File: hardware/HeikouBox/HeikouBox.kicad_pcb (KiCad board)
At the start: 2 copper layers, 100 x 100 mm, 192 parts, among them J101 5V, J201 Conn_02x05_Odd_Even, J202 Conn_02x08_Odd_Even, J301 DB15_Female_HighDensity_Mount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, J302 AudioJack3_SwitchTR, J501 Micro_SD_Card_TFP09-2-12B, J502 RGB, J503 PS/2, Q301 MMBT3904, Q302 MMBT3904, Q303 MMBT3904, Q304 MMBT3904, Q305 MMBT3904, Q306 MMBT3904, Q307 MMBT3904, Q501 BSS138, Q502 BSS138, Q503 BSS138, SW501 Left, SW502 Up, SW503 Down, SW504 Right, U101 LD1117S33TR, U102 LD1117S25TR, U103 LD1117S12TR, U201 HeikouBox-Core, U202 74HCU04, U401 K4S281632-UC60, U501 STM32-BluePill-Socket, Y201 14.31818MHz, Y202 28.37516MHz

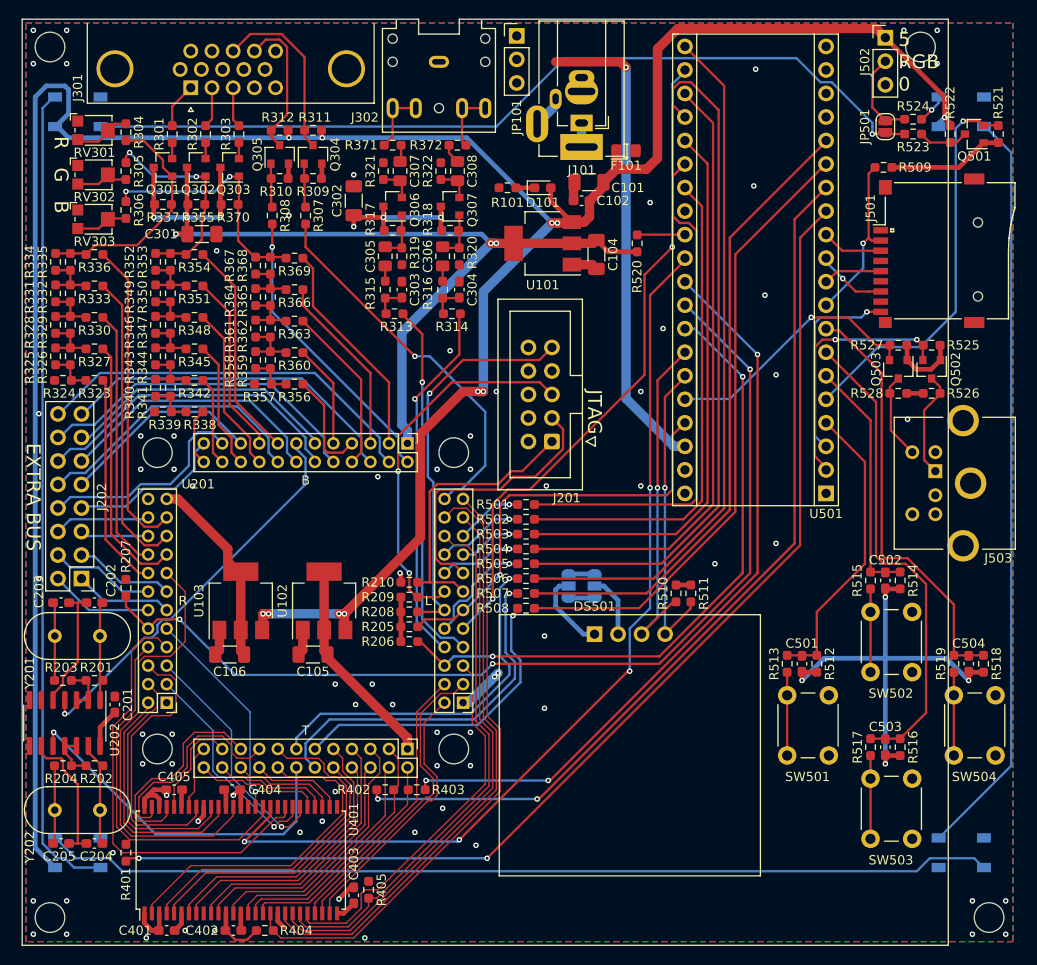
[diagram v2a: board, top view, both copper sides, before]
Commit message: Rerouted some logic
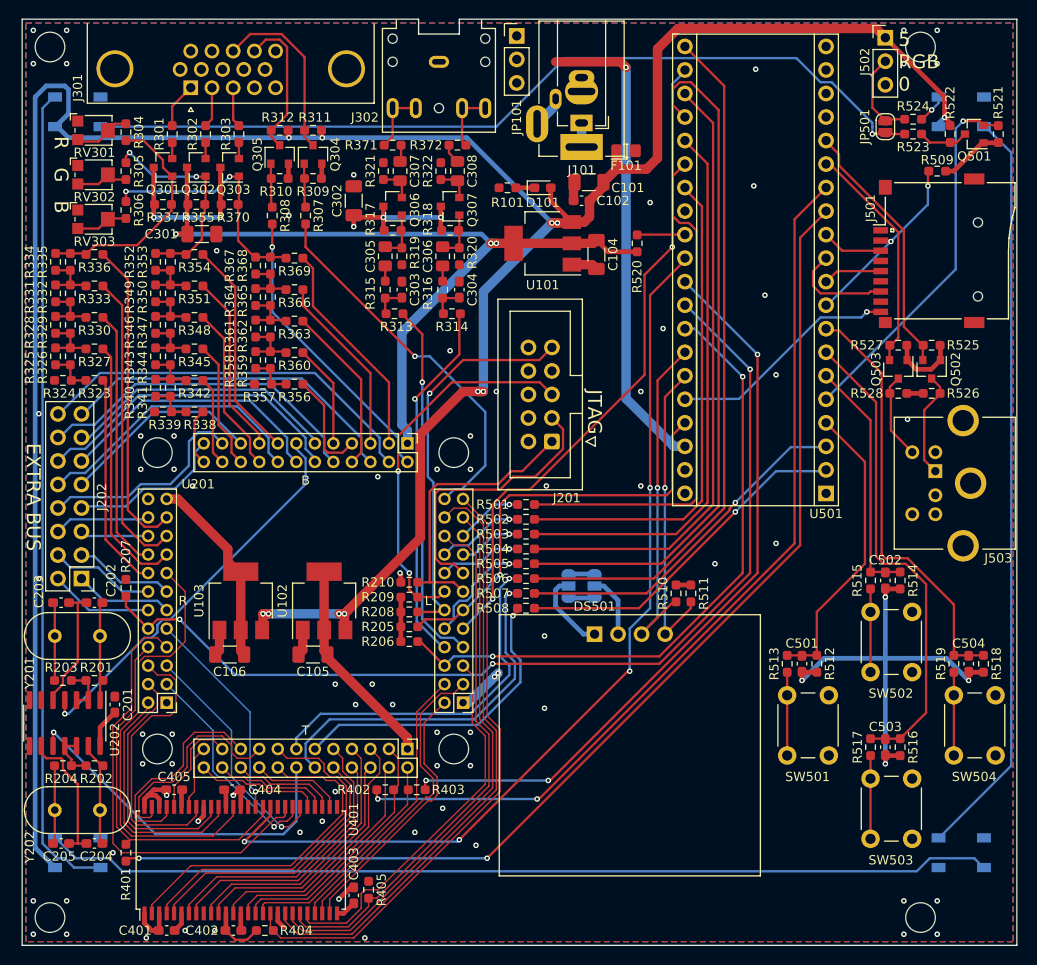
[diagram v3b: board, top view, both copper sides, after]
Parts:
- moved MH4 7.40 mm to (185.8, 153.8)
- moved R509 5.81 mm to (187.6, 73.2)
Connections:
- U501 pad 15: Net-(R508-Pad1) -> Net-(Q503-Pad2)
- U501 pad 16: Net-(R507-Pad1) -> Net-(Q502-Pad2)
- U501 pad 2: Net-(Q502-Pad2) -> Net-(R508-Pad1)
- U501 pad 3: Net-(J501-Pad9) -> Net-(R507-Pad1)
- U501 pad 36: Net-(Q503-Pad2) -> Net-(J501-Pad9)
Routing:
- net Net-(R507-Pad1): track 69.0 -> 38.3 mm, vias 0 -> 1
- net Net-(R508-Pad1): track 67.6 -> 37.7 mm, vias 0 -> 1
- net /part1-power/3V3: track 214.7 -> 209.0 mm
- net Net-(J501-Pad7): track 7.63 -> 11.3 mm, vias 1 -> 0
- net Net-(J501-Pad9): track 21.5 -> 25.1 mm
- net Net-(Q503-Pad2): track 28.6 -> 25.1 mm, vias 1 -> 0
- net Net-(Q501-Pad2): track 42.9 -> 40.2 mm
- net Net-(J501-Pad2): track 18.5 -> 20.3 mm, vias 1 -> 2
- net Net-(Q502-Pad2): track 27.6 -> 28.2 mm, vias 2 -> 0
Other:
- board size 100 x 100 mm -> 107.4 x 100 mm

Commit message: Mainboard v0.1 PCB ready for export
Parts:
- removed the C502 at (182.0, 117.4)
- removed J502: RGB, Connector_PinHeader_2.54mm:PinHeader_1x03_P2.54mm_Vertical
- removed JP101: Power, Connector_PinHeader_2.54mm:PinHeader_1x03_P2.54mm_Vertical
- removed JP501: RGB Bypass, Jumper:SolderJumper-2_P1.3mm_Open_RoundedPad1.0x1.5mm
- removed Q501: BSS138, Package_TO_SOT_SMD:SOT-23
- removed R401, R402, R403, R404, R405: 1K, Resistor_SMD:R_0603_1608Metric_Pad0.98x0.95mm_HandSolder
- removed the R516 at (183.6, 135.4)
- removed the R517 at (180.4, 135.4)
- added C504: 100n, Capacitor_SMD:C_0603_1608Metric_Pad1.08x0.95mm_HandSolder, F.Cu at (174.2, 146.6)
- added D102: D, Diode_SMD:D_SOD-123, F.Cu at (141.6, 63.8)
- added D103: 5.6V, Diode_SMD:D_SOD-123, F.Cu at (169.6, 80.4)
- added F102: Poly 200mA, Fuse:Fuse_0805_2012Metric_Pad1.15x1.40mm_HandSolder, F.Cu at (141.6, 59.4)
- added R518: 10K, Resistor_SMD:R_0603_1608Metric_Pad0.98x0.95mm_HandSolder, F.Cu at (172.4, 148.2)
- added R519: 1K, Resistor_SMD:R_0603_1608Metric_Pad0.98x0.95mm_HandSolder, F.Cu at (170.8, 146.6)
- added R529: 100R, Resistor_SMD:R_0603_1608Metric_Pad0.98x0.95mm_HandSolder, F.Cu at (185.8, 130.8)
- added R530: 1K, Resistor_SMD:R_0603_1608Metric_Pad0.98x0.95mm_HandSolder, F.Cu at (161.2, 118.2)
- added R531: 1K, Resistor_SMD:R_0603_1608Metric_Pad0.98x0.95mm_HandSolder, F.Cu at (159.6, 118.2)
- F101: value Poly 1A -> Poly 2A; footprint Fuse:Fuse_0805_2012Metric_Pad1.15x1.40mm_HandSolder -> Fuse:Fuse_1206_3216Metric_Pad1.42x1.75mm_HandSolder
- R101: value 1K -> 330R
- R520: value RUSB -> 1K5
- R522: value 1K -> 10K
- R524: value 1K -> 100R
- moved R524 59.6 mm to (185.8, 127.2), turned to 270 degrees
- moved R521 55.6 mm to (138.8, 73.6)
- moved R522 50.8 mm to (138.8, 77.0), turned to 270 degrees
- moved R512 45.2 mm to (137.8, 152.6)
- moved R514 45.2 mm to (155.8, 152.6)
- moved R513 42.5 mm to (139.4, 154.4)
- moved R515 42.5 mm to (157.4, 154.4)
- moved C501 41.6 mm to (139.4, 151.0), turned to 270 degrees
- moved C502 41.6 mm to (157.4, 151.0), turned to 270 degrees
- moved R101 39.4 mm to (180.6, 76.2), turned to 90 degrees
- moved R527 39.0 mm to (179.0, 130.8), turned to 90 degrees
- moved Q503 36.2 mm to (181.6, 130.8), turned to 0 degrees
- moved R525 36.1 mm to (179.0, 127.2), turned to 90 degrees
- moved D101 35.9 mm to (180.6, 79.8), turned to 270 degrees
- moved R523 34.2 mm to (167.8, 98.8), turned to 270 degrees
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- renumbered C504 to C502, R518 to R514, R519 to R515, R514 to R516, R515 to R517, SW504 to SW502, SW502 to SW503, SW503 to SW504
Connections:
- net Net-(J501-Pad3) renamed /part5-hub/SD_MOSI
- net Net-(J501-Pad5) renamed /part5-hub/SD_SCK
- net Net-(J501-Pad7) renamed /part5-hub/SD_MISO
- net Net-(R505-Pad1) renamed /part5-hub/MDB4_CD_R
- net Net-(R520-Pad1) renamed /part5-hub/USB_DP
- C501 pad 1: /part1-power/3V3 -> /part5-hub/3V3_HUB
- C501 pad 2: Net-(C501-Pad2) -> /part5-hub/BUTTON_L
- C502 pad 1: /part1-power/3V3 -> /part5-hub/3V3_HUB
- C502 pad 2: Net-(C504-Pad2) -> /part5-hub/BUTTON_R
- C503 pad 1: /part1-power/3V3 -> /part5-hub/3V3_HUB
- C503 pad 2: Net-(C503-Pad2) -> /part5-hub/BUTTON_U
- D101 pad 2: /part1-power/5V -> /part1-power/3V3
- D501 pad 1: /part1-power/5V -> /part1-power/3V3
- D502 pad 1: /part1-power/5V -> /part1-power/3V3
- D503 pad 1: /part1-power/5V -> /part1-power/3V3
- D504 pad 1: /part1-power/5V -> /part1-power/3V3
- DS501 pad 3: Net-(DS501-Pad3) -> /part5-hub/OLED_SCL
- DS501 pad 4: Net-(DS501-Pad4) -> /part5-hub/OLED_SDA
- F101 pad 1: /part1-power/5V -> Net-(F101-Pad1)
- F101 pad 2: Net-(F101-Pad2) -> /part1-power/5V
- J101 pad 1: Net-(J101-Pad1) -> Net-(F101-Pad1)
- J501 pad 2: Net-(J501-Pad2) -> /part5-hub/SD_SS
- J501 pad 4: /part1-power/3V3 -> /part5-hub/3V3_HUB
- J501 pad 9: Net-(J501-Pad9) -> /part5-hub/SD_DET
- JP502 pad 1: /part1-power/3V3 -> /part5-hub/3V3_HUB
- JP502 pad 2: Net-(DS501-Pad2) -> Net-(DS501-Pad1)
- JP503 pad 2: Net-(DS501-Pad1) -> Net-(DS501-Pad2)
- JP503 pad 3: /part1-power/3V3 -> /part5-hub/3V3_HUB
- Q306 pad 1: Net-(C305-Pad1) -> Net-(C305-Pad2)
- Q306 pad 2: Net-(C307-Pad2) -> Net-(C307-Pad1)
- Q307 pad 1: Net-(C306-Pad1) -> Net-(C306-Pad2)
- Q307 pad 2: Net-(C308-Pad2) -> Net-(C308-Pad1)
- Q502 pad 2: Net-(Q502-Pad2) -> /part5-hub/KEYBOARD_DAT
- Q502 pad 3: Net-(J503-Pad1) -> Net-(Q502-Pad3)
- Q503 pad 2: Net-(Q503-Pad2) -> /part5-hub/KEYBOARD_CLK
- Q503 pad 3: Net-(J503-Pad5) -> Net-(Q503-Pad3)
- R301 pad 1: Net-(J301-Pad1) -> Net-(Q301-Pad2)
- R301 pad 2: Net-(Q301-Pad2) -> Net-(J301-Pad1)
- R302 pad 1: Net-(J301-Pad2) -> Net-(Q302-Pad2)
- R302 pad 2: Net-(Q302-Pad2) -> Net-(J301-Pad2)
- R303 pad 1: Net-(J301-Pad3) -> Net-(Q303-Pad2)
- R303 pad 2: Net-(Q303-Pad2) -> Net-(J301-Pad3)
- R307 pad 1: Net-(Q304-Pad1) -> /part3-av/NHSYNC
- R307 pad 2: /part3-av/NHSYNC -> Net-(Q304-Pad1)
- R308 pad 1: Net-(Q305-Pad1) -> /part3-av/NVSYNC
- R308 pad 2: /part3-av/NVSYNC -> Net-(Q305-Pad1)
- R309 pad 1: /part1-power/GND -> Net-(Q304-Pad1)
- R309 pad 2: Net-(Q304-Pad1) -> /part1-power/GND
- R310 pad 1: /part1-power/GND -> Net-(Q305-Pad1)
- R310 pad 2: Net-(Q305-Pad1) -> /part1-power/GND
- R311 pad 1: Net-(J301-Pad13) -> /part1-power/3V3
- R311 pad 2: /part1-power/5V -> Net-(J301-Pad13)
- R312 pad 1: Net-(J301-Pad14) -> /part1-power/3V3
- R312 pad 2: /part1-power/5V -> Net-(J301-Pad14)
- R313 pad 1: Net-(C303-Pad1) -> /part3-av/LSIGMA
- R313 pad 2: /part3-av/LSIGMA -> Net-(C303-Pad1)
- R314 pad 1: Net-(C304-Pad1) -> /part3-av/RSIGMA
- R314 pad 2: /part3-av/RSIGMA -> Net-(C304-Pad1)
- R315 pad 1: Net-(C305-Pad2) -> Net-(C303-Pad1)
- R315 pad 2: Net-(C303-Pad1) -> Net-(C305-Pad1)
- R316 pad 1: Net-(C306-Pad2) -> Net-(C304-Pad1)
- R316 pad 2: Net-(C304-Pad1) -> Net-(C306-Pad1)
- R317 pad 2: Net-(C305-Pad1) -> Net-(C305-Pad2)
- R318 pad 2: Net-(C306-Pad1) -> Net-(C306-Pad2)
- R319 pad 1: Net-(C305-Pad1) -> Net-(C305-Pad2)
- R320 pad 1: Net-(C306-Pad1) -> Net-(C306-Pad2)
- R321 pad 1: Net-(C307-Pad2) -> Net-(C307-Pad1)
- R322 pad 1: Net-(C308-Pad2) -> Net-(C308-Pad1)
- R371 pad 1: Net-(J302-PadT) -> Net-(C307-Pad2)
- R371 pad 2: Net-(C307-Pad1) -> Net-(J302-PadT)
- R372 pad 1: Net-(J302-PadR) -> Net-(C308-Pad2)
- R372 pad 2: Net-(C308-Pad1) -> Net-(J302-PadR)
- R501 pad 1: Net-(R501-Pad1) -> /part5-hub/MDB0_RX_R
- R502 pad 1: Net-(R502-Pad1) -> /part5-hub/MDB1_TX_R
- R503 pad 1: Net-(R503-Pad1) -> /part5-hub/MDB2_R
- R504 pad 1: Net-(R504-Pad1) -> /part5-hub/MDB3_R
- R506 pad 1: Net-(R506-Pad1) -> /part5-hub/MDB5_R
- R507 pad 1: Net-(R507-Pad1) -> /part5-hub/MDB6_R
- R508 pad 1: Net-(R508-Pad1) -> /part5-hub/MDB7_R
- R509 pad 1: Net-(J501-Pad2) -> /part5-hub/3V3_HUB
- R509 pad 2: /part1-power/3V3 -> /part5-hub/SD_SS
- R510 pad 1: Net-(DS501-Pad3) -> /part5-hub/OLED_SCL
- R510 pad 2: /part1-power/3V3 -> /part5-hub/3V3_HUB
- R511 pad 1: Net-(DS501-Pad4) -> /part5-hub/OLED_SDA
- R511 pad 2: /part1-power/3V3 -> /part5-hub/3V3_HUB
- R512 pad 1: /part1-power/3V3 -> Net-(R512-Pad1)
- R512 pad 2: Net-(C501-Pad2) -> /part5-hub/3V3_HUB
- R513 pad 1: Net-(R513-Pad1) -> Net-(R512-Pad1)
- R513 pad 2: Net-(C501-Pad2) -> /part5-hub/BUTTON_L
- R514 pad 1: /part1-power/3V3 -> Net-(R514-Pad1)
- R514 pad 2: Net-(C504-Pad2) -> /part5-hub/3V3_HUB
- R515 pad 1: Net-(R519-Pad1) -> Net-(R514-Pad1)
- R515 pad 2: Net-(C504-Pad2) -> /part5-hub/BUTTON_R
- R516 pad 1: /part1-power/3V3 -> Net-(R516-Pad1)
- R516 pad 2: Net-(C502-Pad2) -> /part5-hub/3V3_HUB
- R517 pad 1: Net-(R515-Pad1) -> Net-(R516-Pad1)
- R517 pad 2: Net-(C502-Pad2) -> /part5-hub/BUTTON_U
- R520 pad 2: /part1-power/3V3 -> /part5-hub/3V3_HUB
- R521 pad 1: Net-(Q501-Pad2) -> /part1-power/3V3
- R521 pad 2: /part1-power/3V3 -> /part5-hub/PWR_DET
- R522 pad 1: Net-(Q501-Pad3) -> /part5-hub/PWR_DET
- R522 pad 2: /part1-power/5V -> /part1-power/GND
- R523 pad 1: Net-(Q501-Pad3) -> /part5-hub/NEOPIXEL
- R524 pad 1: Net-(D504-Pad2) -> Net-(Q502-Pad3)
- R524 pad 2: Net-(J502-Pad2) -> Net-(J503-Pad1)
- R525 pad 1: Net-(Q502-Pad2) -> /part5-hub/KEYBOARD_DAT
- R526 pad 1: Net-(J503-Pad1) -> Net-(Q502-Pad3)
- R527 pad 1: Net-(Q503-Pad2) -> /part5-hub/KEYBOARD_CLK
- R528 pad 1: Net-(J503-Pad5) -> Net-(Q503-Pad3)
- SW501 pad 1: Net-(R513-Pad1) -> Net-(R512-Pad1)
- SW502 pad 1: Net-(R519-Pad1) -> Net-(R514-Pad1)
- SW503 pad 1: Net-(R515-Pad1) -> Net-(R516-Pad1)
- U401 pad 37: /part4-memory/CKE -> /part1-power/3V3
- U501 pad 13: /part4-memory/XCLK -> /part5-hub/BUTTON_L
- U501 pad 14: /part4-memory/XWE -> /part5-hub/BUTTON_R
- U501 pad 15: Net-(Q503-Pad2) -> /part5-hub/BUTTON_U
- U501 pad 16: Net-(Q502-Pad2) -> /part5-hub/BUTTON_D
- U501 pad 2: Net-(R508-Pad1) -> Net-(U501-Pad2)
- U501 pad 21: Net-(R506-Pad1) -> /part2-core/cfg_NCFG
- U501 pad 23: Net-(R504-Pad1) -> /part5-hub/CFG_DONE_R
- U501 pad 25: Net-(R503-Pad1) -> /part5-hub/SD_DET
- U501 pad 26: Net-(R501-Pad1) -> /part5-hub/PWR_DET
- U501 pad 27: Net-(R502-Pad1) -> /part5-hub/MDB2_R
- U501 pad 3: Net-(R507-Pad1) -> Net-(U501-Pad3)
- U501 pad 30: /part4-memory/CKE -> /part5-hub/MDB3_R
- U501 pad 31: /part4-memory/XCAS -> /part5-hub/MDB5_R
- U501 pad 32: /part2-core/cfg_DONE -> /part5-hub/MDB6_R
- U501 pad 33: /part2-core/cfg_NSTAT -> /part5-hub/MDB7_R
- U501 pad 34: Net-(DS501-Pad3) -> /part5-hub/MDB0_RX_R
- U501 pad 35: Net-(DS501-Pad4) -> /part5-hub/MDB1_TX_R
- U501 pad 36: Net-(J501-Pad9) -> /part5-hub/OLED_SCL
- U501 pad 37: /part2-core/cfg_NCFG -> /part5-hub/OLED_SDA
- U501 pad 4: Net-(C501-Pad2) -> Net-(U501-Pad4)
- U501 pad 40: Net-(U501-Pad40) -> /part5-hub/3V3_HUB
- U501 pad 5: Net-(Q501-Pad2) -> /part5-hub/NEOPIXEL
- U501 pad 6: Net-(C502-Pad2) -> /part5-hub/KEYBOARD_DAT
- U501 pad 7: Net-(C503-Pad2) -> /part5-hub/KEYBOARD_CLK
- U501 pad 8: Net-(C504-Pad2) -> /part5-hub/CFG_NSTAT_R
- U501 pad 9: Net-(J501-Pad2) -> /part5-hub/SD_SS
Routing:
- net /part1-power/3V3: track 209.0 -> 533.3 mm, vias 13 -> 28
- net /part5-hub/3V3_HUB: track 0.00 -> 196.8 mm, vias 0 -> 10
- net /part4-memory/XCLK: track 124.2 -> 0.00 mm, vias 2 -> 0
- net /part4-memory/CKE: track 101.2 -> 0.00 mm, vias 4 -> 0
- net /part4-memory/XWE: track 97.3 -> 0.00 mm, vias 2 -> 0
- net /part5-hub/BUTTON_L: track 0.00 -> 92.1 mm, vias 0 -> 1
- net /part5-hub/BUTTON_R: track 0.00 -> 87.7 mm, vias 0 -> 1
- net /part5-hub/BUTTON_D: track 0.00 -> 82.7 mm, vias 0 -> 1
- net /part1-power/5V: track 295.6 -> 213.0 mm, vias 11 -> 7
- net /part4-memory/XCAS: track 80.8 -> 0.00 mm, vias 3 -> 0
- net Net-(R506-Pad1): track 75.2 -> 0.00 mm
- net Net-(R504-Pad1): track 66.9 -> 0.00 mm
- net /part5-hub/BUTTON_U: track 0.00 -> 63.6 mm, vias 0 -> 1
- net /part5-hub/SD_DET: track 0.00 -> 60.4 mm, vias 0 -> 1
- net Net-(R503-Pad1): track 60.2 -> 0.00 mm
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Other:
- board size 107.4 x 100 mm -> 100 x 100 mm
- board text added: "5V 2A"
- board text added: "GND VCC"
- board text added: "HeikouBox"
- board text added: "JLCJLCJLCJLC"
- board text added: "LINE AUD"
- board text added: "Mainboard v0.1 KasamiKona 2022"
- board text added: "SD CARD"
- board text added: "VGA VIDEO"
- board text removed: "5 RGB 0"
- board text removed: "5V 1A"
- board text removed: "LINE OUT"
- board text removed: "MICRO SD"
- board text removed: "VCC GND"
- board text removed: "VGA"

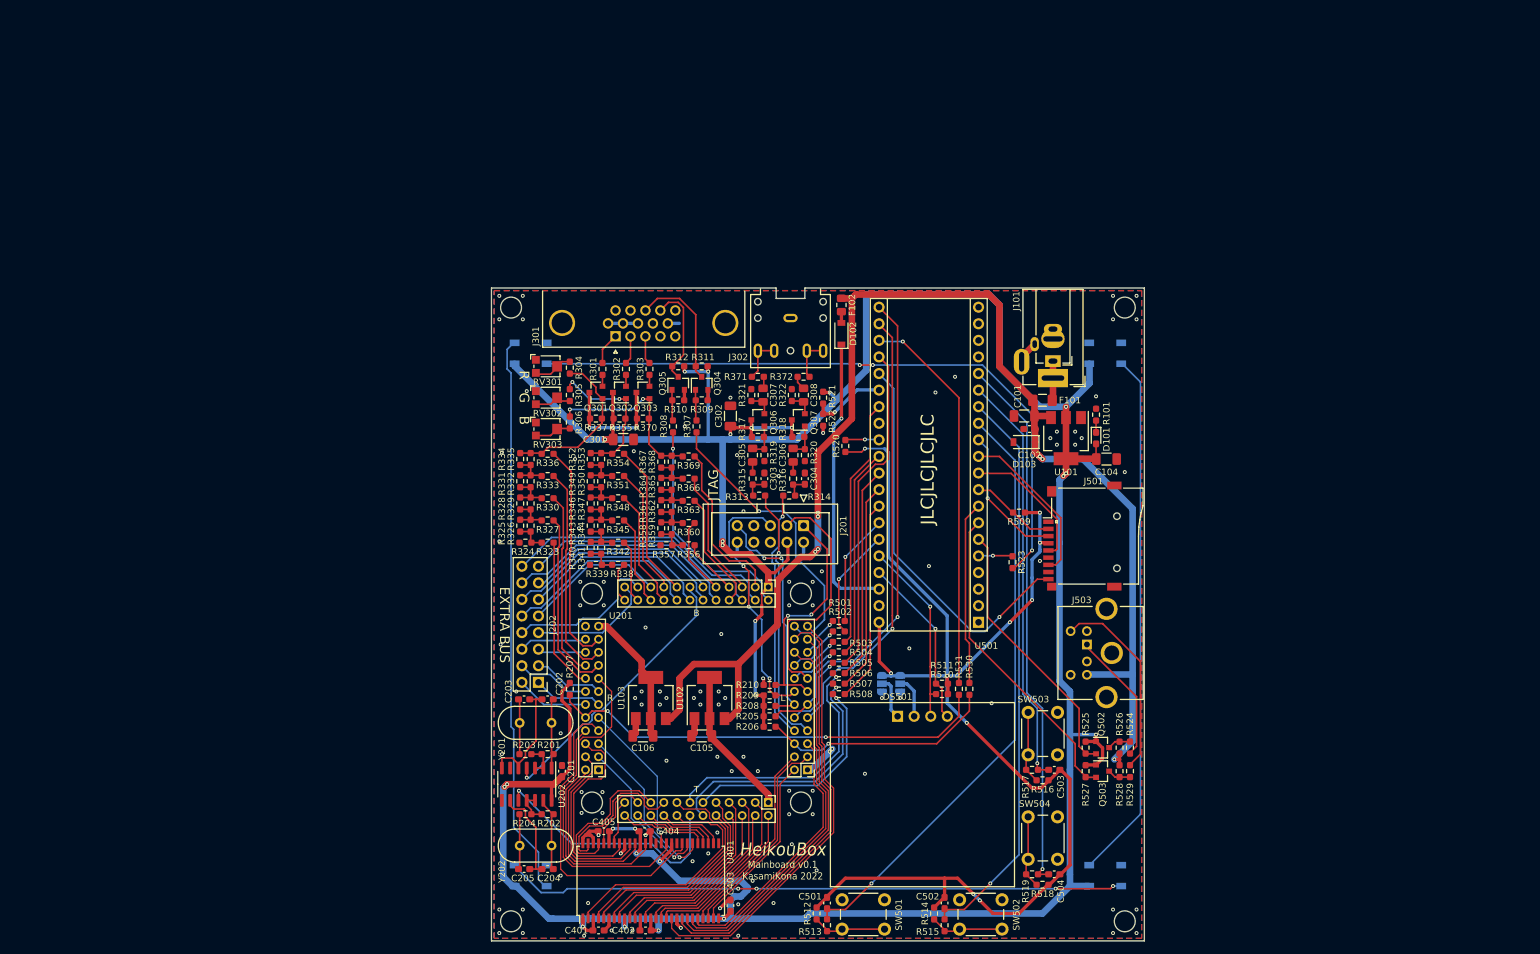
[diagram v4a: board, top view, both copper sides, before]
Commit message: Move board near origin
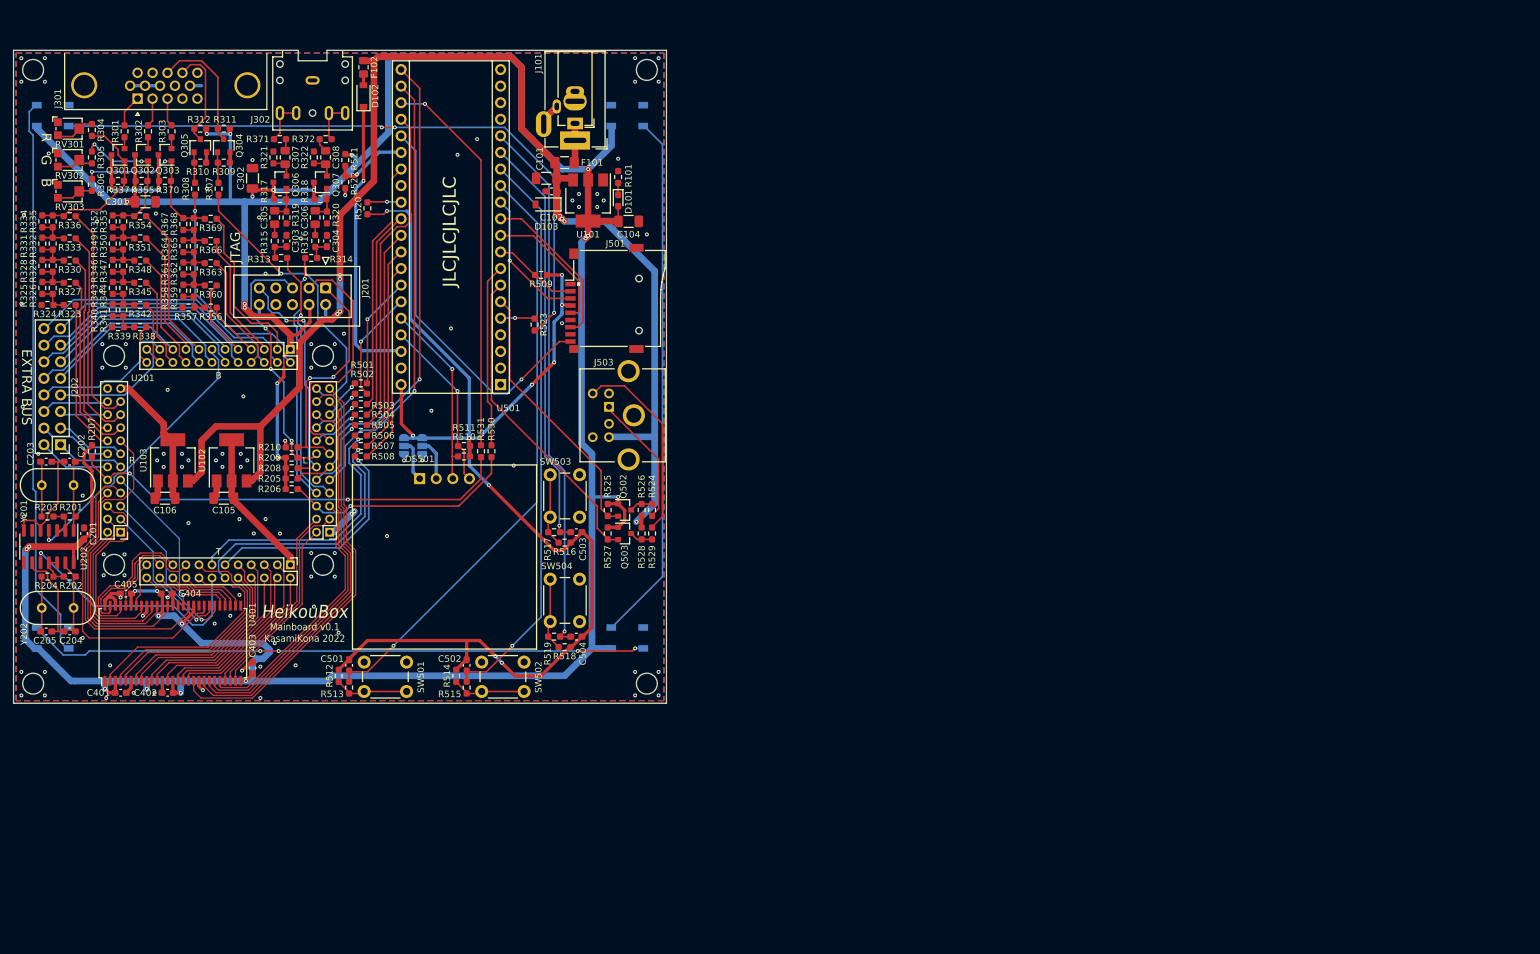
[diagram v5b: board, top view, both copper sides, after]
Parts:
- moved C308 81.8 mm to (62.6, 36.8)
- moved J201 81.8 mm to (62.6, 56.8)
- moved JP502 81.8 mm to (74.6, 81.0)
- moved R319 81.8 mm to (56.6, 46.0)
- moved R371 81.8 mm to (55.6, 34.0)
- moved R372 81.8 mm to (62.6, 34.0)
- moved R509 81.8 mm to (95.6, 54.8)
- moved R524 81.8 mm to (112.6, 90.8)
- moved R529 81.8 mm to (112.6, 94.4)
- moved C102 81.8 mm to (97.2, 42.0)
- moved C105 81.8 mm to (47.0, 89.0)
- moved C106 81.8 mm to (38.0, 89.0)
- moved C205 81.8 mm to (19.8, 109.4)
- moved C301 81.8 mm to (35.0, 43.6)
- moved C303 81.8 mm to (56.6, 49.6)
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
